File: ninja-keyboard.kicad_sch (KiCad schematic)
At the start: 265 parts, among them J1 Conn_01x05_Pin, J3 USB_C_Receptacle_USB2.0_14P, J4 Conn_01x02, Q1 SS8050, Q2 AO3401A, SW1 backquote, SW10 num9, SW11 num0, SW12 -, SW13 =, SW14 backsapce, SW15 tab, SW16 q, SW17 w, SW18 e, SW19 r, SW2 num1, SW20 t, SW21 y, SW22 u, SW23 i, SW24 o, SW25 p, SW26 [, SW27 ], SW28 \, SW29 cap, SW3 num2, SW30 a, SW31 s, SW32 d, SW33 f, SW34 h, SW35 g, SW36 j, SW37 k, SW38 l, SW39 semicolon, SW4 num3, SW40 apostrophe, SW41 enter, SW42 lshift, SW43 z, SW44 x, SW45 c, SW46 v, SW47 b, SW48 n, SW49 m, SW5 num4, SW50 comma, SW51 period, SW52 /, SW53 rshift, SW54 lctrl, SW55 win, SW56 lalt, SW57 space, SW58 ralt, SW59 win, SW6 num5, SW60 menu, SW61 rctrl, SW62 RotaryEncoder, SW63 SW_SPDT, SW7 num6, SW8 num7, SW9 num8, U1 ESP32-S3-WROOM-1, U2 TP4056-42-ESOP8

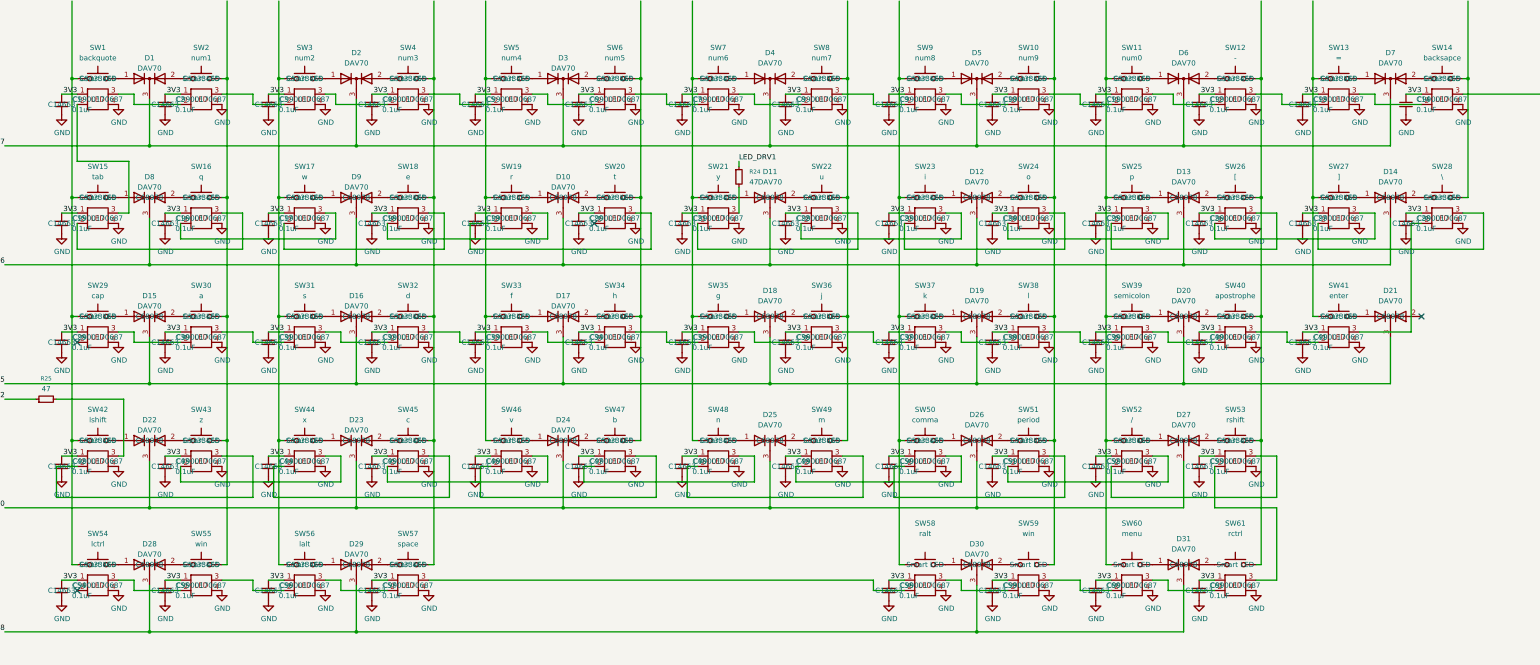
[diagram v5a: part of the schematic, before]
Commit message: Fix position output of switches and smart leds to correct side
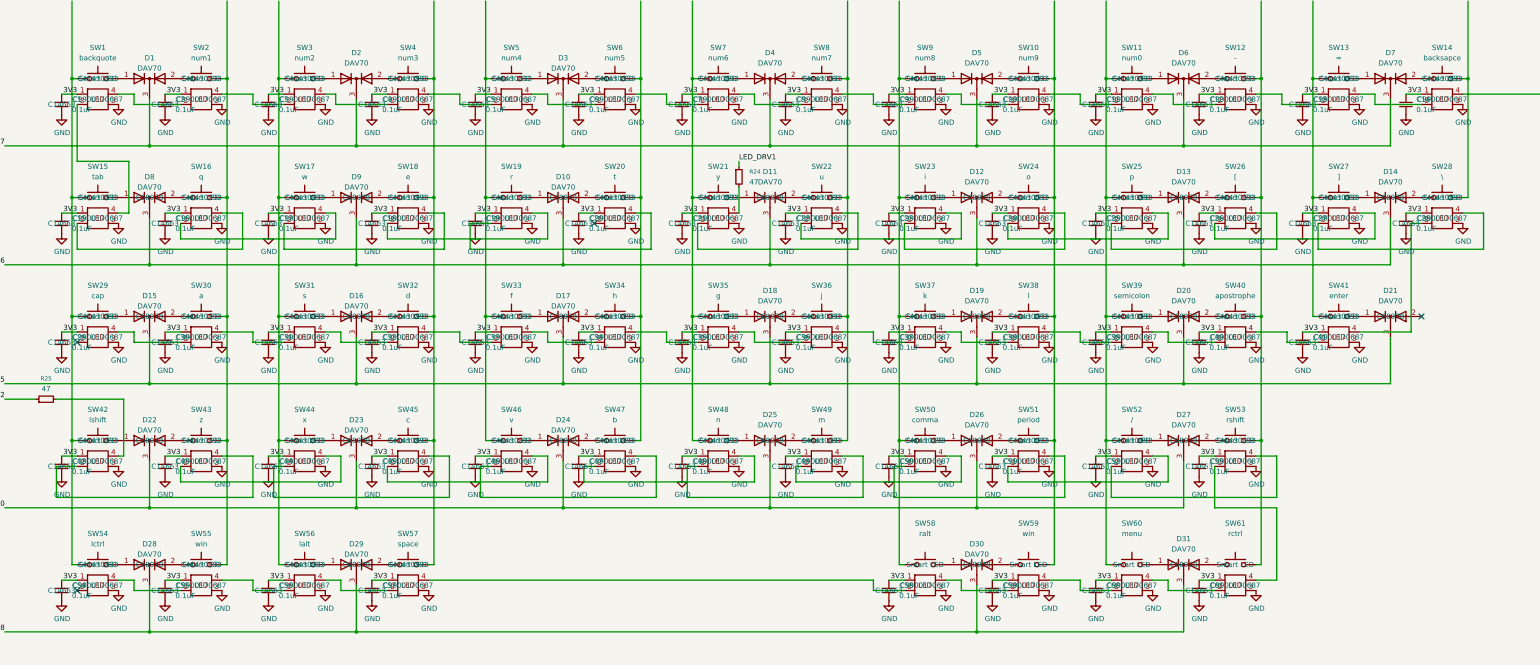
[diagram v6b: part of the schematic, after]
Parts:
- SW1, SW10, SW11, SW12, SW13, SW16, SW17, SW18, SW19, SW2, SW20, SW21, SW22, SW23, SW24, SW25, SW26, SW27, SW3, SW30, SW31, SW32, SW33, SW34, SW35, SW36, SW37, SW38, SW39, SW4, SW40, SW43, SW44, SW45, SW46, SW47, SW48, SW49, SW5, SW50, SW51, SW52, SW6, SW7, SW8, SW9: footprint PCM_Switch_Keyboard_Hotswap_Kailh:SW_Hotswap_Kailh_MX_1.00u -> user_added:SW_Hotswap_Kailh_MX_1.00u_reversed; LCSC Part # C5333465 -> C41430893
- SW14: footprint PCM_Switch_Keyboard_Hotswap_Kailh:SW_Hotswap_Kailh_MX_2.00u -> user_added:SW_Hotswap_Kailh_MX_2.00u_reversed; LCSC Part # C5333465 -> C41430893
- SW15, SW28: footprint PCM_Switch_Keyboard_Hotswap_Kailh:SW_Hotswap_Kailh_MX_1.50u -> user_added:SW_Hotswap_Kailh_MX_1.50u_reversed; LCSC Part # C5333465 -> C41430893
- SW29: footprint PCM_Switch_Keyboard_Hotswap_Kailh:SW_Hotswap_Kailh_MX_1.75u -> user_added:SW_Hotswap_Kailh_MX_1.75u_reversed; LCSC Part # C5333465 -> C41430893
- SW41, SW42: footprint PCM_Switch_Keyboard_Hotswap_Kailh:SW_Hotswap_Kailh_MX_2.25u -> user_added:SW_Hotswap_Kailh_MX_2.25u_reversed; LCSC Part # C5333465 -> C41430893
- SW53: footprint PCM_Switch_Keyboard_Hotswap_Kailh:SW_Hotswap_Kailh_MX_2.75u -> user_added:SW_Hotswap_Kailh_MX_2.75u_reversed; LCSC Part # C5333465 -> C41430893
- SW54, SW55, SW56, SW58, SW59, SW60, SW61: footprint PCM_Switch_Keyboard_Hotswap_Kailh:SW_Hotswap_Kailh_MX_1.25u -> user_added:SW_Hotswap_Kailh_MX_1.25u_reversed; LCSC Part # C5333465 -> C41430893
- SW57: footprint PCM_Switch_Keyboard_Hotswap_Kailh:SW_Hotswap_Kailh_MX_6.25u -> user_added:SW_Hotswap_Kailh_MX_6.25u_reversed; LCSC Part # C5333465 -> C41430893
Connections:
- net GND: now also SL1.3 (GND), SL10.3 (GND), SL11.3 (GND), SL12.3 (GND), SL13.3 (GND), SL14.3 (GND), SL15.3 (GND), SL16.3 (GND), SL17.3 (GND), SL18.3 (GND), SL19.3 (GND), SL2.3 (GND), SL20.3 (GND), SL21.3 (GND), SL22.3 (GND), SL23.3 (GND), SL24.3 (GND), SL25.3 (GND), SL26.3 (GND), SL27.3 (GND), SL28.3 (GND), SL29.3 (GND), SL3.3 (GND), SL30.3 (GND), SL31.3 (GND), SL32.3 (GND), SL33.3 (GND), SL34.3 (GND), SL35.3 (GND), SL36.3 (GND), SL37.3 (GND), SL38.3 (GND), SL39.3 (GND), SL4.3 (GND), SL40.3 (GND), SL41.3 (GND), SL42.3 (GND), SL43.3 (GND), SL44.3 (GND), SL45.3 (GND), SL46.3 (GND), SL47.3 (GND), SL48.3 (GND), SL49.3 (GND), SL5.3 (GND), SL50.3 (GND), SL51.3 (GND), SL52.3 (GND), SL53.3 (GND), SL54.3 (GND), SL55.3 (GND), SL56.3 (GND), SL57.3 (GND), SL58.3 (GND), SL59.3 (GND), SL6.3 (GND), SL60.3 (GND), SL61.3 (GND), SL7.3 (GND), SL8.3 (GND), SL9.3 (GND); no longer SL1.4 (GND), SL10.4 (GND), SL11.4 (GND), SL12.4 (GND), SL13.4 (GND), SL14.4 (GND), SL15.4 (GND), SL16.4 (GND), SL17.4 (GND), SL18.4 (GND), SL19.4 (GND), SL2.4 (GND), SL20.4 (GND), SL21.4 (GND), SL22.4 (GND), SL23.4 (GND), SL24.4 (GND), SL25.4 (GND), SL26.4 (GND), SL27.4 (GND), SL28.4 (GND), SL29.4 (GND), SL3.4 (GND), SL30.4 (GND), SL31.4 (GND), SL32.4 (GND), SL33.4 (GND), SL34.4 (GND), SL35.4 (GND), SL36.4 (GND), SL37.4 (GND), SL38.4 (GND), SL39.4 (GND), SL4.4 (GND), SL40.4 (GND), SL41.4 (GND), SL42.4 (GND), SL43.4 (GND), SL44.4 (GND), SL45.4 (GND), SL46.4 (GND), SL47.4 (GND), SL48.4 (GND), SL49.4 (GND), SL5.4 (GND), SL50.4 (GND), SL51.4 (GND), SL52.4 (GND), SL53.4 (GND), SL54.4 (GND), SL55.4 (GND), SL56.4 (GND), SL57.4 (GND), SL58.4 (GND), SL59.4 (GND), SL6.4 (GND), SL60.4 (GND), SL61.4 (GND), SL7.4 (GND), SL8.4 (GND), SL9.4 (GND)
- net at SL30.2 (DOUT): now also SL29.4 (DIN); no longer SL29.3 (DIN)
- net at SL31.2 (DOUT): now also SL30.4 (DIN); no longer SL30.3 (DIN)
- net at R24.2: now also SL21.4 (DIN); no longer SL21.3 (DIN)
- net at SL13.2 (DOUT): now also SL12.4 (DIN); no longer SL12.3 (DIN)
- net at SL14.2 (DOUT): now also SL13.4 (DIN); no longer SL13.3 (DIN)
- net at SL48.2 (DOUT): now also SL49.4 (DIN); no longer SL49.3 (DIN)
- net at SL47.2 (DOUT): now also SL48.4 (DIN); no longer SL48.3 (DIN)
- net at SL59.2 (DOUT): now also SL58.4 (DIN); no longer SL58.3 (DIN)
- net at SL60.2 (DOUT): now also SL59.4 (DIN); no longer SL59.3 (DIN)
- net at SL55.2 (DOUT): now also SL54.4 (DIN); no longer SL54.3 (DIN)
- net at SL45.2 (DOUT): now also SL46.4 (DIN); no longer SL46.3 (DIN)
- net at SL44.2 (DOUT): now also SL45.4 (DIN); no longer SL45.3 (DIN)
- net at SL15.2 (DOUT): now also SL16.4 (DIN); no longer SL16.3 (DIN)
- net at SL1.2 (DOUT): now also SL15.4 (DIN); no longer SL15.3 (DIN)
- net at SL42.2 (DOUT): now also SL43.4 (DIN); no longer SL43.3 (DIN)
- net at R25.2: now also SL42.4 (DIN); no longer SL42.3 (DIN)
- net at R1.1: now also SL14.4 (DIN); no longer SL14.3 (DIN)
- net at SL3.2 (DOUT): now also SL2.4 (DIN); no longer SL2.3 (DIN)
- net at SL4.2 (DOUT): now also SL3.4 (DIN); no longer SL3.3 (DIN)
- net at SL61.2 (DOUT): now also SL60.4 (DIN); no longer SL60.3 (DIN)
- net at SL53.2 (DOUT): now also SL61.4 (DIN); no longer SL61.3 (DIN)
- net at SL39.2 (DOUT): now also SL38.4 (DIN); no longer SL38.3 (DIN)
- net at SL40.2 (DOUT): now also SL39.4 (DIN); no longer SL39.3 (DIN)
- net at SL51.2 (DOUT): now also SL52.4 (DIN); no longer SL52.3 (DIN)
- net at SL50.2 (DOUT): now also SL51.4 (DIN); no longer SL51.3 (DIN)
- net at SL46.2 (DOUT): now also SL47.4 (DIN); no longer SL47.3 (DIN)
- net at SL12.2 (DOUT): now also SL11.4 (DIN); no longer SL11.3 (DIN)
- net at SL56.2 (DOUT): now also SL55.4 (DIN); no longer SL55.3 (DIN)
- net at SL49.2 (DOUT): now also SL50.4 (DIN); no longer SL50.3 (DIN)
- net at SL8.2 (DOUT): now also SL7.4 (DIN); no longer SL7.3 (DIN)
- net at SL9.2 (DOUT): now also SL8.4 (DIN); no longer SL8.3 (DIN)
- net at SL43.2 (DOUT): now also SL44.4 (DIN); no longer SL44.3 (DIN)
- net at SL2.2 (DOUT): now also SL1.4 (DIN); no longer SL1.3 (DIN)
- net at SL28.2 (DOUT): now also SL41.4 (DIN); no longer SL41.3 (DIN)
- net at SL27.2 (DOUT): now also SL28.4 (DIN); no longer SL28.3 (DIN)
- net at SL41.2 (DOUT): now also SL40.4 (DIN); no longer SL40.3 (DIN)
- net at SL16.2 (DOUT): now also SL17.4 (DIN); no longer SL17.3 (DIN)
- net at SL22.2 (DOUT): now also SL23.4 (DIN); no longer SL23.3 (DIN)
- net at SL21.2 (DOUT): now also SL22.4 (DIN); no longer SL22.3 (DIN)
- net at SL37.2 (DOUT): now also SL36.4 (DIN); no longer SL36.3 (DIN)
- net at SL38.2 (DOUT): now also SL37.4 (DIN); no longer SL37.3 (DIN)
- net at SL36.2 (DOUT): now also SL35.4 (DIN); no longer SL35.3 (DIN)
- net at SL5.2 (DOUT): now also SL4.4 (DIN); no longer SL4.3 (DIN)
- net at SL6.2 (DOUT): now also SL5.4 (DIN); no longer SL5.3 (DIN)
- net at SL26.2 (DOUT): now also SL27.4 (DIN); no longer SL27.3 (DIN)
- net at SL35.2 (DOUT): now also SL34.4 (DIN); no longer SL34.3 (DIN)
- net at SL7.2 (DOUT): now also SL6.4 (DIN); no longer SL6.3 (DIN)
- net at SL52.2 (DOUT): now also SL53.4 (DIN); no longer SL53.3 (DIN)
- net at SL34.2 (DOUT): now also SL33.4 (DIN); no longer SL33.3 (DIN)
- net at SL25.2 (DOUT): now also SL26.4 (DIN); no longer SL26.3 (DIN)
- net at SL24.2 (DOUT): now also SL25.4 (DIN); no longer SL25.3 (DIN)
- net at SL11.2 (DOUT): now also SL10.4 (DIN); no longer SL10.3 (DIN)
- net at SL19.2 (DOUT): now also SL20.4 (DIN); no longer SL20.3 (DIN)
- net at SL32.2 (DOUT): now also SL31.4 (DIN); no longer SL31.3 (DIN)
- net at SL18.2 (DOUT): now also SL19.4 (DIN); no longer SL19.3 (DIN)
- net at SL17.2 (DOUT): now also SL18.4 (DIN); no longer SL18.3 (DIN)
- net at SL10.2 (DOUT): now also SL9.4 (DIN); no longer SL9.3 (DIN)
- net at SL23.2 (DOUT): now also SL24.4 (DIN); no longer SL24.3 (DIN)
- net at SL33.2 (DOUT): now also SL32.4 (DIN); no longer SL32.3 (DIN)
- net at SL57.2 (DOUT): now also SL56.4 (DIN); no longer SL56.3 (DIN)
- net at SL58.2 (DOUT): now also SL57.4 (DIN); no longer SL57.3 (DIN)

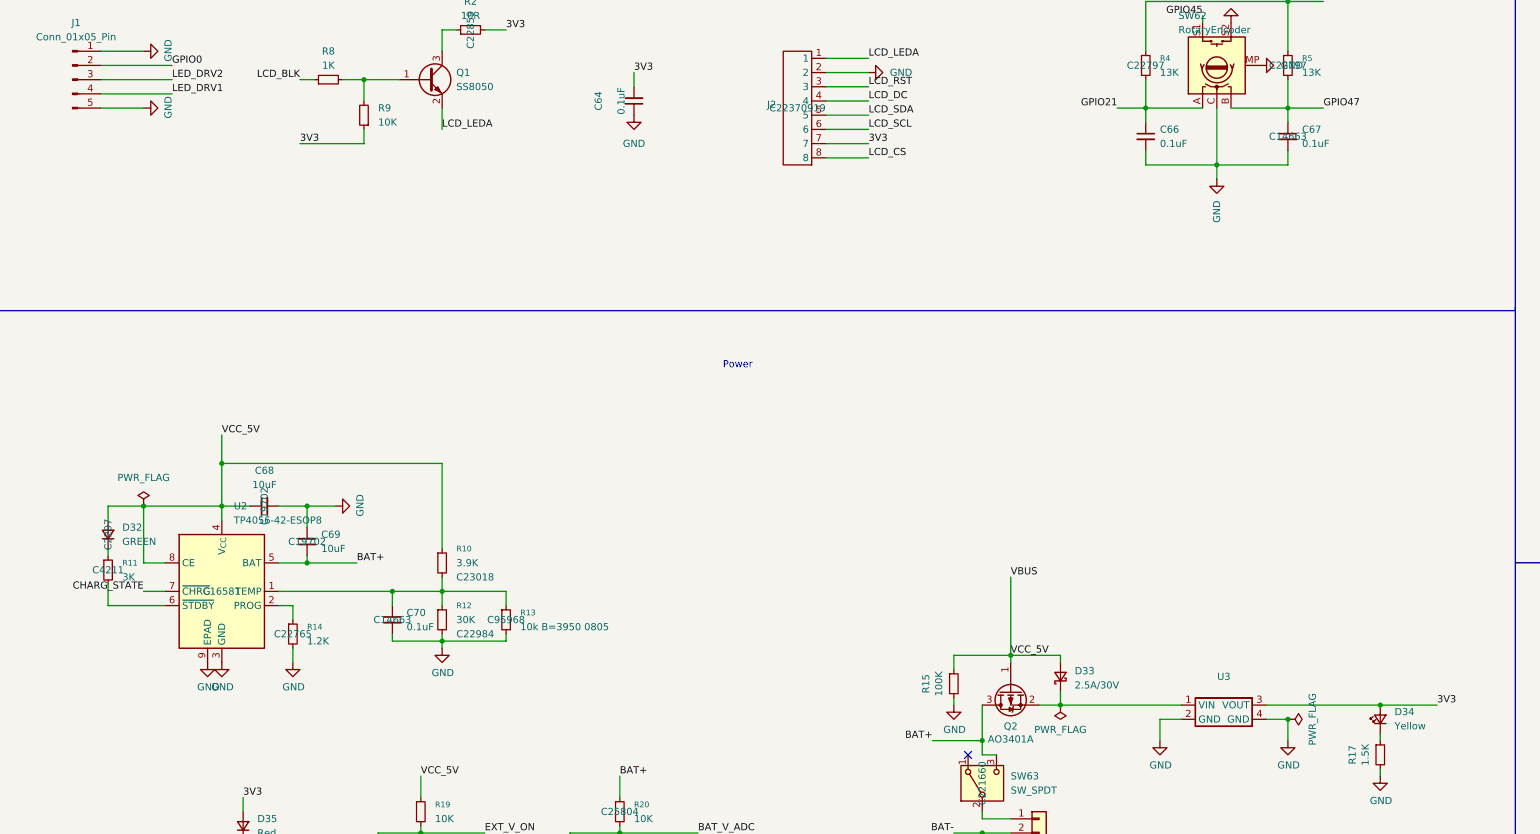
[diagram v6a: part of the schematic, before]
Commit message: Fix some LSCS# Numbers
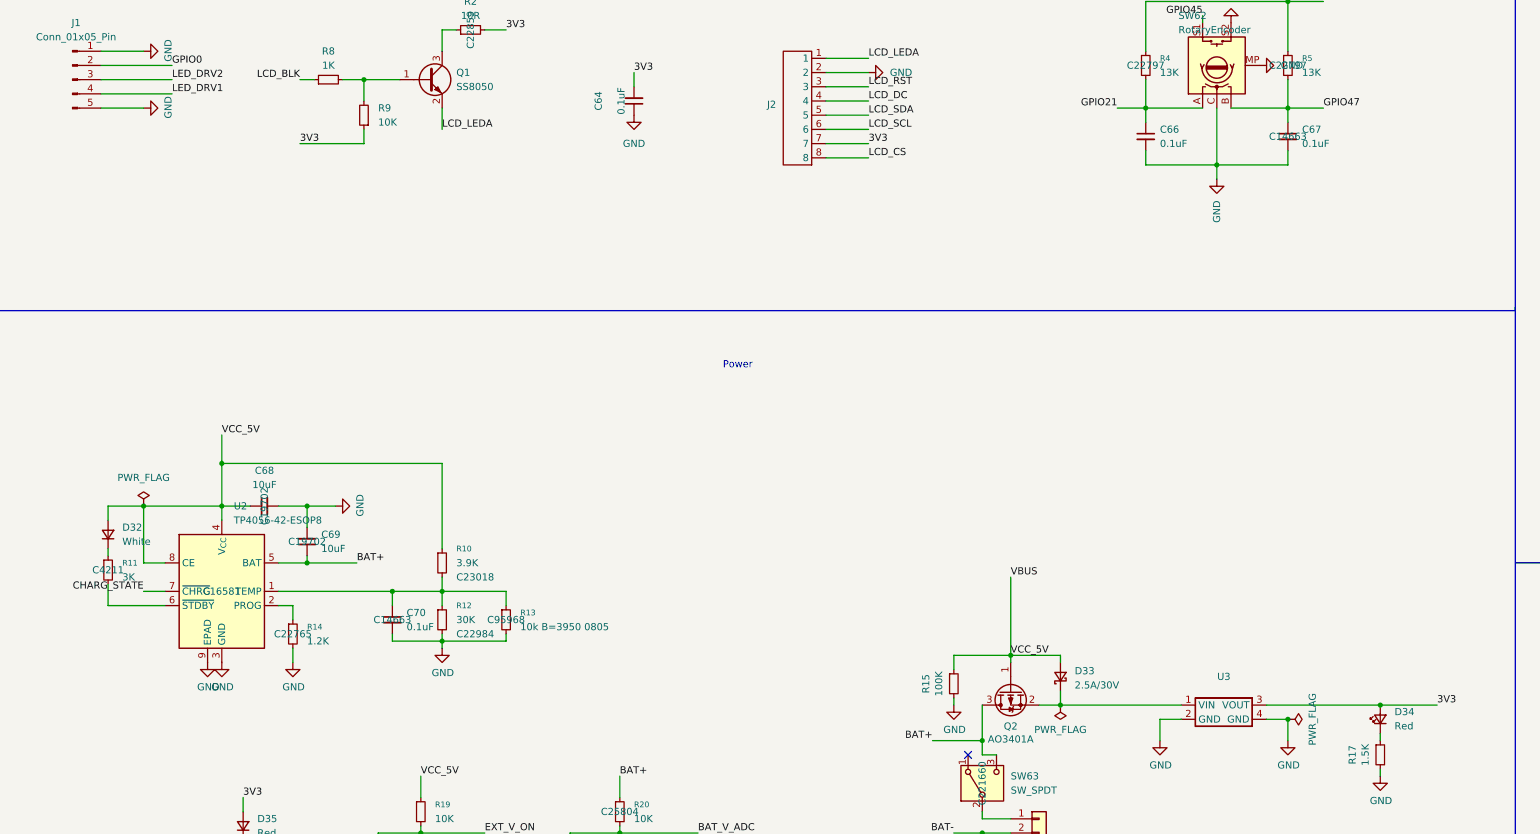
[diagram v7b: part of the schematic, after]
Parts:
- D32: value GREEN -> White; LCSC Part # C2297 -> C2290
- D34: value Yellow -> Red; LCSC Part # C2296 -> C2286
- J2: LCSC Part # C22370919 -> C22435652
- J4: LCSC Part # C2845379 -> C7527581
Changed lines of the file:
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@@
 			)
 		)
-		(property "LCSC Part #" "C2845379"
+		(property "LCSC Part #" "C7527581"
 			(at 199.39 375.92 0)
 			(effects
@@
 			)
 		)
-		(property "Value" "GREEN"
+		(property "Value" "White"
 			(at 35.56 326.3899 90)
 			(effects
@@
 			)
 		)
-		(property "LCSC Part #" "C2297"
+		(property "LCSC Part #" "C2290"
 			(at 33.02 325.12 0)
 			(effects
@@
 					(size 1.27 1.27)
 				)
+				(hide yes)
 			)
 		)
@@
 			)
 		)
-		(property "LCSC Part #" "C22370919"
+		(property "LCSC Part #" "C22435652"
 			(at 156.21 248.92 0)
 			(effects
@@
 					(size 1.27 1.27)
 				)
+				(hide yes)
 			)
 		)
@@
 			)
 		)
-		(property "Value" "Yellow"
+		(property "Value" "Red"
 			(at 262.89 359.3464 90)
 			(effects
@@
 			)
 		)
-		(property "LCSC Part #" "C2296"
+		(property "LCSC Part #" "C2286"
 			(at 260.35 358.14 0)
 			(effects
